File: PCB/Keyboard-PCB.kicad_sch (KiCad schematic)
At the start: 57 parts, among them J1 USB_C_Receptacle_USB2.0_16P, J2 BOOT0, J3 BOOT1, J4 BOOT0, J5 BOOT1, J6 Debug UART, J7 Debug UART, SW43 SW_Push, SW44 SW_Push, U1 AMS1117-3.3, U2 STM32F103C8Tx, U3 STM32F103C8Tx

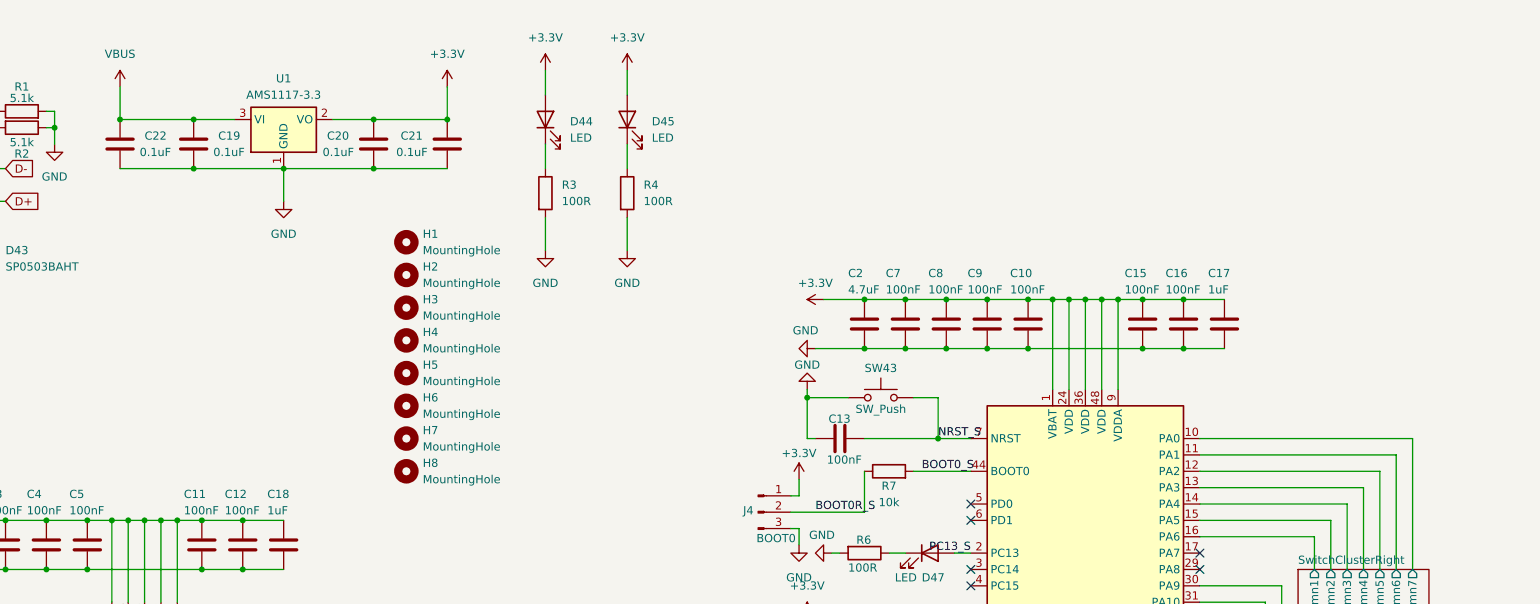
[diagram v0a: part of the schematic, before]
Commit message: Add more mounting holes and do some cad work
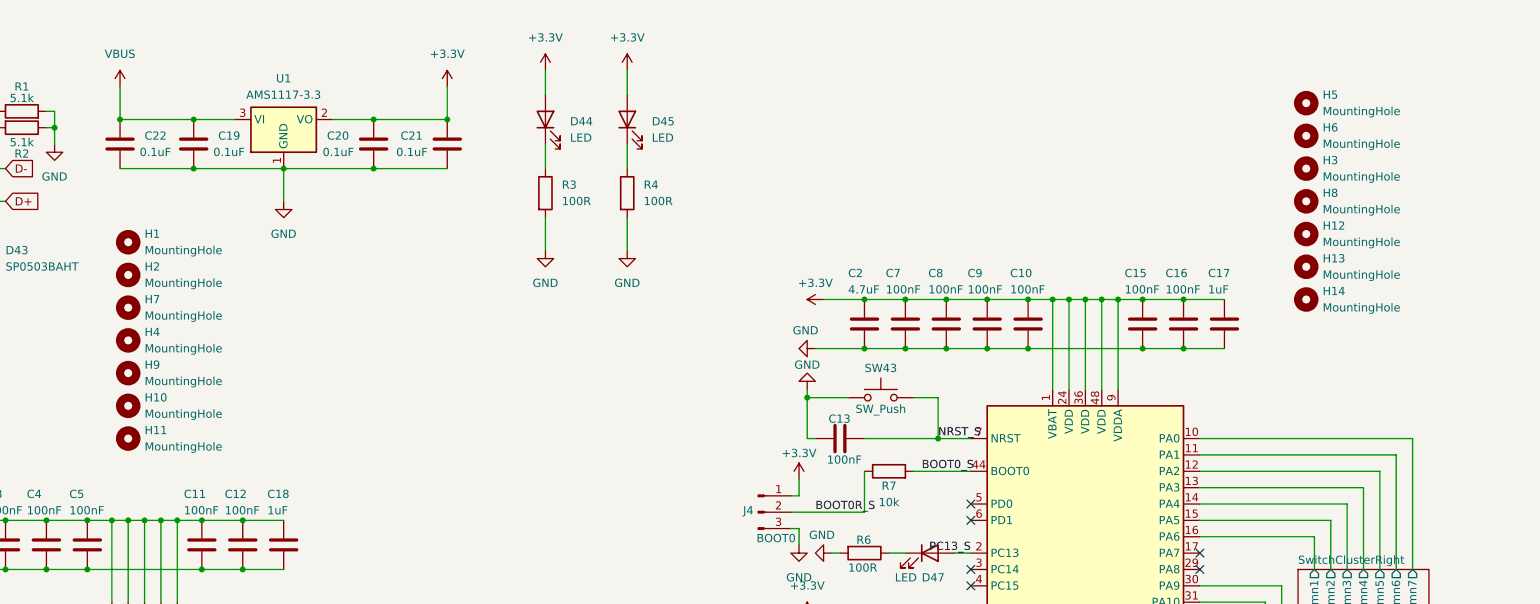
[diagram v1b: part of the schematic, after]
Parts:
- added H10, H11, H12, H13, H14, H9: MountingHole, MountingHole:MountingHole_3mm, symbol Mechanical:MountingHole
- renumbered H2 to H1, H3 to H2, H5 to H3, H7 to H4, H1 to H5, H4 to H6, H6 to H7
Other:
- moved on the sheet: H1, H2, H3, H4, H5, H6, H7, H8
